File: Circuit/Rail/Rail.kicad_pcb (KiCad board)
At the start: 2 copper layers, 49.5 x 33 mm, 10 parts, among them J1 Coil Power, J2 Trigger, Q1 70PT12DS

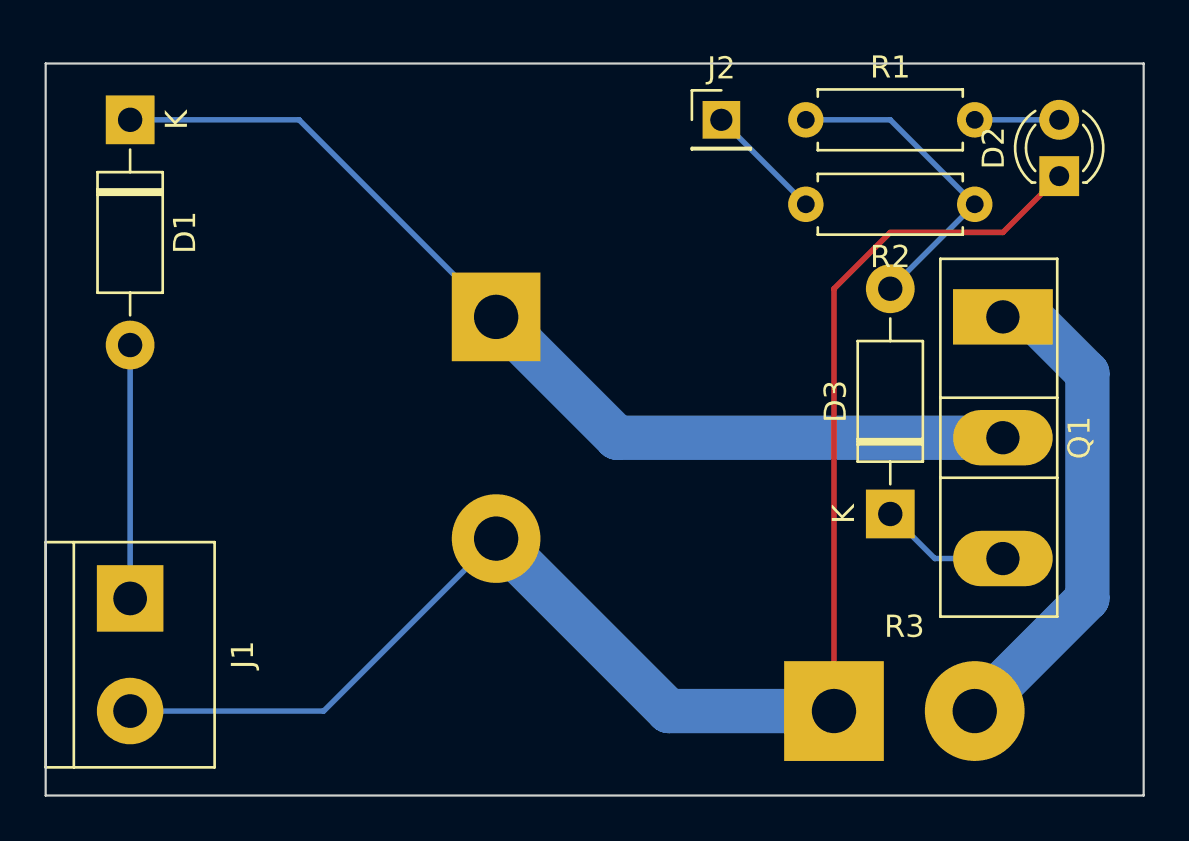
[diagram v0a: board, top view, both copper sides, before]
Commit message: [Circuit] Update circuit files to KiCAD 6's
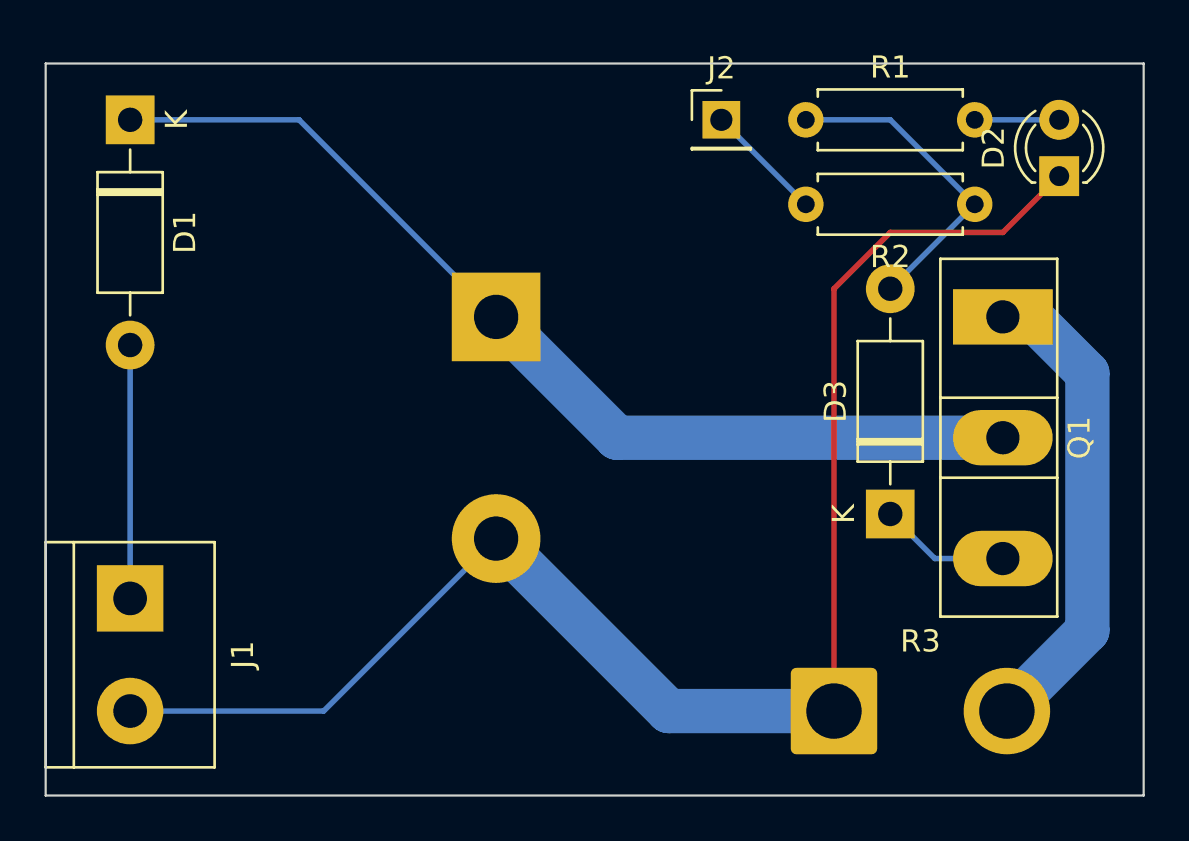
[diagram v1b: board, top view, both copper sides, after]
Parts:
- R3: footprint Connector_Wire:SolderWirePad_1x02_P7.62mm_Drill2mm -> Connector_Wire:SolderWire-2sqmm_1x02_P7.8mm_D2mm_OD3.9mm
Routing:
- net Net-(Q1-Pad1): track 22.2 -> 21.6 mm
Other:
- net class Default removed
